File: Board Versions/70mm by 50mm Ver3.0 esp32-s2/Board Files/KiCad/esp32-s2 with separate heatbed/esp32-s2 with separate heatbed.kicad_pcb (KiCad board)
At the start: 2 copper layers, 65.5 x 50 mm, 59 parts, among them IC1 ESP32-S2FN4R2, J1 PJ-037B, J2 USB4520-03-0-A, J3 TB003-500-P02BE, J4 TB003-500-P02BE, J5 Conn_01x03_Male, Q1 PJD25N06A_L2_00001, U1 LD1117S33TR_SOT223, U2 MAX31855KASA, Y1 ECS-400-15-33B-CTN-TR

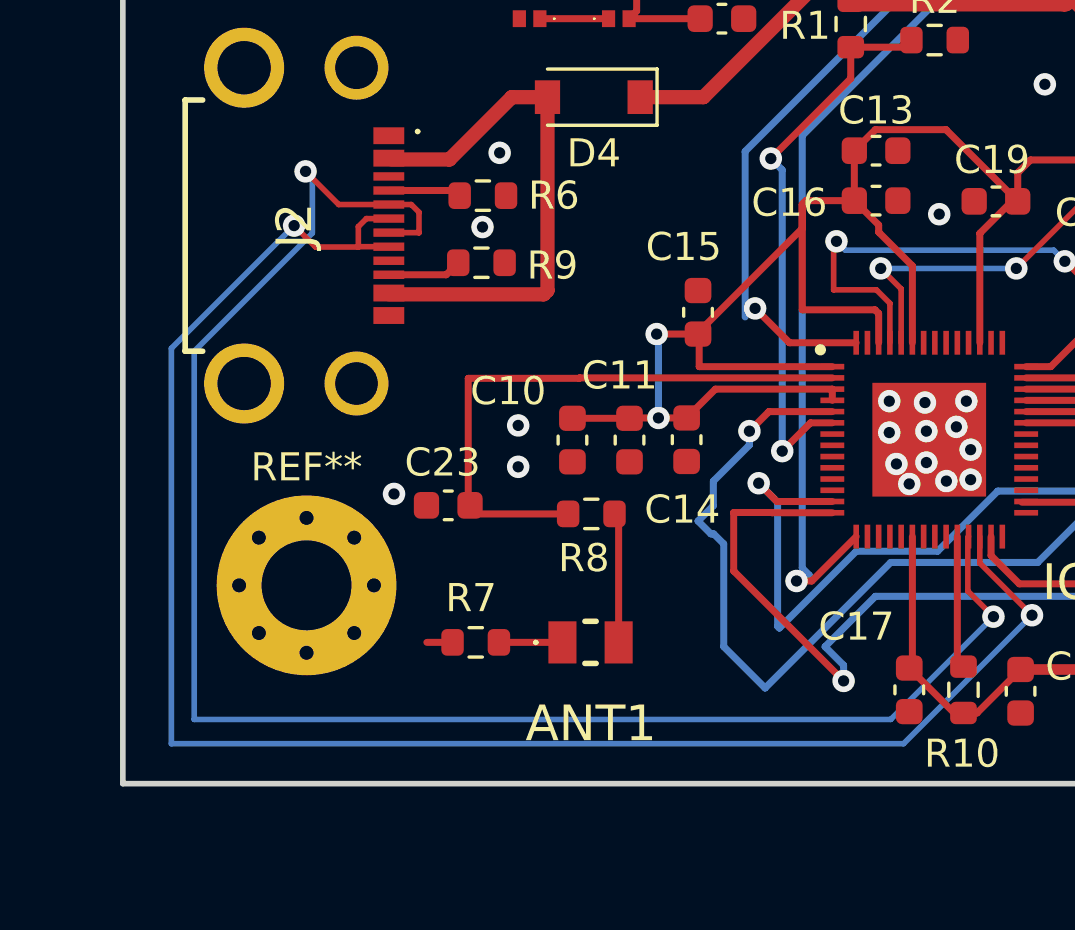
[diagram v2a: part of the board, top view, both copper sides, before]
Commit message: Move antenna to edge
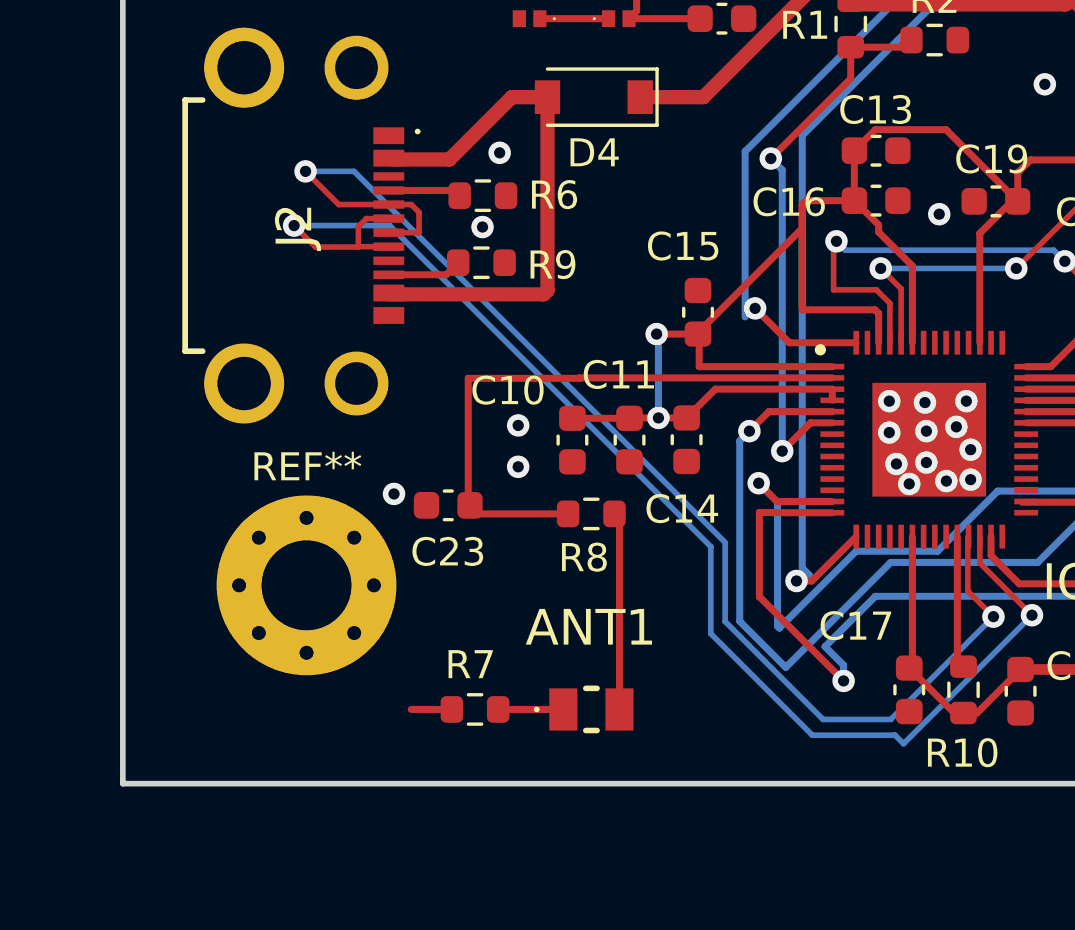
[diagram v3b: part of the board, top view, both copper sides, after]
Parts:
- moved ANT1 2.39 mm to (30.1, 61.4)
- moved R7 2.39 mm to (26.0, 61.4)
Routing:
- net D-: track 61.0 -> 45.4 mm
- net D+: track 62.0 -> 46.8 mm
- net FLASH: track 55.0 -> 52.3 mm
- net Net-(ANT1-Pad2): track 4.63 -> 7.03 mm
- net led2: track 58.2 -> 56.9 mm
- net GND: track 6.17 -> 6.70 mm
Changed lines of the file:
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@@
   )
   (footprint "library_manager:21088321" (layer "F.Cu")
-    (at 30.1084 59.0296)
+    (at 30.1404 61.4172)
     (descr "2108832-1-2")
     (tags "Antenna")
@@
     (property "Sheetname" "")
     (attr smd)
-    (fp_text reference "ANT1" (at 0.016 2.8956) (layer "F.SilkS")
+    (fp_text reference "ANT1" (at -0.016 -2.8956) (layer "F.SilkS")
       (effects (font (size 1.27 1.27) (thickness 0.254)))
     )
@@
       (effects (font (size 1.27 1.27) (thickness 0.254)))
     )
-    (fp_text user "${REFERENCE}" (at 3.7752 -0.0508 90) (layer "F.Fab")
+    (fp_text user "${REFERENCE}" (at 3.6416 -0.4064 90) (layer "F.Fab")
       (effects (font (size 1.27 1.27) (thickness 0.254)))
     )
@@
   )
   (footprint "Resistor_SMD:R_0603_1608Metric" (layer "F.Cu")
-    (at 26.0218 59.0296 180)
+    (at 25.9974 61.4172 180)
     (descr "Resistor SMD 0603 (1608 Metric), square (rectangular) end terminal, IPC_7351 nominal, (Body size source: IPC-SM-782 page 72, https://www.pcb-3d.com/wordpress/wp-content/uploads/ipc-sm-782a_amendment_1_and_2.pdf), generated with kicad-footprint-generator")
     (tags "resistor")
@@
     (property "Sheetname" "")
     (attr smd)
-    (fp_text reference "C23" (at 0.2032 1.524) (layer "F.SilkS")
+    (fp_text reference "C23" (at 0 -1.6764) (layer "F.SilkS")
       (effects (font (size 1 1) (thickness 0.15)))
     )
@@
     (effects (font (size 1.5 1.5) (thickness 0.3)))
   )
-  (segment (start 29.1084 59.0296) (end 26.8468 59.0296) (width 0.25) (layer "F.Cu") (net 1))
-  (segment (start 30.9616 54.4576) (end 31.1084 54.6044) (width 0.25) (layer "F.Cu") (net 2))
-  (segment (start 31.1084 54.6044) (end 31.1084 59.0296) (width 0.25) (layer "F.Cu") (net 2))
+  (segment (start 29.1404 61.4172) (end 26.8224 61.4172) (width 0.25) (layer "F.Cu") (net 1))
+  (segment (start 30.9616 54.4576) (end 31.1404 54.6364) (width 0.25) (layer "F.Cu") (net 2))
+  (segment (start 31.1404 54.6364) (end 31.1404 61.4172) (width 0.25) (layer "F.Cu") (net 2))
   (segment (start 31.75 36.56) (end 31.48 36.83) (width 0.25) (layer "F.Cu") (net 3))
   (segment (start 41.403 28.702) (end 39.37 30.735) (width 1.524) (layer "F.Cu") (net 3))
@@
   (segment (start 32.11 30.86) (end 31.75 30.5) (width 1.27) (layer "F.Cu") (net 3))
   (segment (start 53.608 46.482) (end 53.208 46.482) (width 0.25) (layer "F.Cu") (net 4))
+  (segment (start 25.1724 61.4172) (end 23.7236 61.4172) (width 0.25) (layer "F.Cu") (net 4))
   (segment (start 63.0428 45.9232) (end 62.3824 45.2628) (width 0.25) (layer "F.Cu") (net 4))
-  (segment (start 25.1968 59.0296) (end 24.2824 59.0296) (width 0.25) (layer "F.Cu") (net 4))
   (segment (start 62.3824 44.2468) (end 62.5348 44.0944) (width 0.25) (layer "F.Cu") (net 4))
   (segment (start 53.208 46.482) (end 51.308 44.582) (width 0.25) (layer "F.Cu") (net 4))
@@
   (via (at 35.7632 51.5112) (size 0.8) (drill 0.4) (layers "F.Cu" "B.Cu") (net 17))
   (via (at 63.6016 52.0192) (size 0.8) (drill 0.4) (layers "F.Cu" "B.Cu") (net 17))
-  (segment (start 33.9344 54.7116) (end 34.3916 55.1688) (width 0.25) (layer "B.Cu") (net 17))
+  (segment (start 37.0586 59.9186) (end 40.7924 56.1848) (width 0.25) (layer "B.Cu") (net 17))
+  (segment (start 61.556289 54.064511) (end 63.6016 52.0192) (width 0.25) (layer "B.Cu") (net 17))
+  (segment (start 35.419689 58.279689) (end 37.0586 59.9186) (width 0.25) (layer "B.Cu") (net 17))
+  (segment (start 35.7632 51.5112) (end 35.419689 51.854711) (width 0.25) (layer "B.Cu") (net 17))
+  (segment (start 48.145089 54.064511) (end 61.556289 54.064511) (width 0.25) (layer "B.Cu") (net 17))
+  (segment (start 46.0248 56.1848) (end 48.145089 54.064511) (width 0.25) (layer "B.Cu") (net 17))
+  (segment (start 35.419689 51.854711) (end 35.419689 58.279689) (width 0.25) (layer "B.Cu") (net 17))
   (segment (start 40.7924 56.1848) (end 46.0248 56.1848) (width 0.25) (layer "B.Cu") (net 17))
-  (segment (start 35.7632 51.5112) (end 35.7632 52.006772) (width 0.25) (layer "B.Cu") (net 17))
-  (segment (start 34.3916 55.1688) (end 34.4932 55.1688) (width 0.25) (layer "B.Cu") (net 17))
-  (segment (start 35.7632 52.006772) (end 34.479889 53.290083) (width 0.25) (layer "B.Cu") (net 17))
-  (segment (start 36.322 60.6552) (end 40.7924 56.1848) (width 0.25) (layer "B.Cu") (net 17))
-  (segment (start 48.145089 54.064511) (end 61.556289 54.064511) (width 0.25) (layer "B.Cu") (net 17))
-  (segment (start 34.479889 53.290083) (end 34.479889 54.166111) (width 0.25) (layer "B.Cu") (net 17))
-  (segment (start 34.479889 54.166111) (end 33.9344 54.7116) (width 0.25) (layer "B.Cu") (net 17))
-  (segment (start 61.556289 54.064511) (end 63.6016 52.0192) (width 0.25) (layer "B.Cu") (net 17))
-  (segment (start 34.8488 55.5244) (end 34.8488 59.182) (width 0.25) (layer "B.Cu") (net 17))
-  (segment (start 34.8488 59.182) (end 36.322 60.6552) (width 0.25) (layer "B.Cu") (net 17))
-  (segment (start 46.0248 56.1848) (end 48.145089 54.064511) (width 0.25) (layer "B.Cu") (net 17))
-  (segment (start 34.4932 55.1688) (end 34.8488 55.5244) (width 0.25) (layer "B.Cu") (net 17))
   (segment (start 39.37 38.9636) (end 36.5252 41.8084) (width 0.25) (layer "F.Cu") (net 18))
   (segment (start 39.37 37.845) (end 39.37 38.9636) (width 0.25) (layer "F.Cu") (net 18))
@@
   (segment (start 39.56552 55.78608) (end 36.83 58.5216) (width 0.25) (layer "B.Cu") (net 25))
   (segment (start 68.7324 35.2552) (end 66.7512 35.2552) (width 0.25) (layer "B.Cu") (net 25))
-  (segment (start 35.2044 54.4068) (end 35.2044 56.4896) (width 0.25) (layer "F.Cu") (net 26))
+  (segment (start 36.1188 54.4068) (end 36.1188 57.404) (width 0.25) (layer "F.Cu") (net 26))
+  (segment (start 38.714 54.416) (end 36.5668 54.416) (width 0.25) (layer "F.Cu") (net 26))
   (segment (start 66.6232 39.5224) (end 68.6308 39.5224) (width 0.25) (layer "F.Cu") (net 26))
   (segment (start 68.6308 39.5224) (end 68.7324 39.4208) (width 0.25) (layer "F.Cu") (net 26))
+  (segment (start 36.1188 57.404) (end 39.116 60.4012) (width 0.25) (layer "F.Cu") (net 26))
+  (segment (start 36.5576 54.4068) (end 36.1188 54.4068) (width 0.25) (layer "F.Cu") (net 26))
   (segment (start 36.5668 54.416) (end 36.5576 54.4068) (width 0.25) (layer "F.Cu") (net 26))
-  (segment (start 36.5576 54.4068) (end 35.2044 54.4068) (width 0.25) (layer "F.Cu") (net 26))
-  (segment (start 35.2044 56.4896) (end 39.116 60.4012) (width 0.25) (layer "F.Cu") (net 26))
-  (segment (start 38.714 54.416) (end 36.5668 54.416) (width 0.25) (layer "F.Cu") (net 26))
   (via (at 39.116 60.4012) (size 0.8) (drill 0.4) (layers "F.Cu" "B.Cu") (net 26))
   (via (at 68.7324 39.4208) (size 0.8) (drill 0.4) (layers "F.Cu" "B.Cu") (net 26))
@@
   (via (at 19.9644 42.2656) (size 0.8) (drill 0.4) (layers "F.Cu" "B.Cu") (net 33))
   (segment (start 44.45 58.1152) (end 40.7924 61.7728) (width 0.2) (layer "B.Cu") (net 33))
-  (segment (start 16.002 61.7728) (end 16.002 48.669417) (width 0.2) (layer "B.Cu") (net 33))
-  (segment (start 16.002 48.669417) (end 20.206711 44.464706) (width 0.2) (layer "B.Cu") (net 33))
-  (segment (start 40.7924 61.7728) (end 16.002 61.7728) (width 0.2) (layer "B.Cu") (net 33))
-  (segment (start 20.206711 42.507911) (end 19.9644 42.2656) (width 0.2) (layer "B.Cu") (net 33))
-  (segment (start 20.206711 44.464706) (end 20.206711 42.507911) (width 0.2) (layer "B.Cu") (net 33))
+  (segment (start 34.8996 55.4736) (end 21.6916 42.2656) (width 0.2) (layer "B.Cu") (net 33))
+  (segment (start 21.6916 42.2656) (end 19.9644 42.2656) (width 0.2) (layer "B.Cu") (net 33))
+  (segment (start 40.7924 61.7728) (end 38.38428 61.7728) (width 0.2) (layer "B.Cu") (net 33))
+  (segment (start 34.8996 58.28812) (end 34.8996 55.4736) (width 0.2) (layer "B.Cu") (net 33))
+  (segment (start 38.38428 61.7728) (end 34.8996 58.28812) (width 0.2) (layer "B.Cu") (net 33))
   (segment (start 21.844 44.958) (end 21.856 44.946) (width 0.2) (layer "F.Cu") (net 34))
   (segment (start 22.929 43.946) (end 22.129978 43.946) (width 0.2) (layer "F.Cu") (net 34))
@@
   (via (at 45.8216 58.0644) (size 0.8) (drill 0.4) (layers "F.Cu" "B.Cu") (free) (net 34))
   (via (at 19.558 44.196) (size 0.8) (drill 0.4) (layers "F.Cu" "B.Cu") (net 34))
-  (segment (start 15.1892 62.6364) (end 15.1892 48.5648) (width 0.2) (layer "B.Cu") (net 34))
-  (segment (start 15.1892 48.5648) (end 19.558 44.196) (width 0.2) (layer "B.Cu") (net 34))
-  (segment (start 41.2496 62.6364) (end 15.1892 62.6364) (width 0.2) (layer "B.Cu") (net 34))
+  (segment (start 40.9448 62.3316) (end 37.9984 62.3316) (width 0.2) (layer "B.Cu") (net 34))
+  (segment (start 34.3916 58.7248) (end 34.3916 55.626) (width 0.2) (layer "B.Cu") (net 34))
+  (segment (start 22.9616 44.196) (end 19.558 44.196) (width 0.2) (layer "B.Cu") (net 34))
+  (segment (start 41.2496 62.6364) (end 40.9448 62.3316) (width 0.2) (layer "B.Cu") (net 34))
+  (segment (start 34.3916 55.626) (end 22.9616 44.196) (width 0.2) (layer "B.Cu") (net 34))
+  (segment (start 37.9984 62.3316) (end 34.3916 58.7248) (width 0.2) (layer "B.Cu") (net 34))
   (segment (start 45.8216 58.0644) (end 41.2496 62.6364) (width 0.2) (layer "B.Cu") (net 34))
   (segment (start 54.7212 51.216) (end 45.614 51.216) (width 0.25) (layer "F.Cu") (net 43))
@@
     (polygon
       (pts
-        (xy 24.4348 55.2196)
-        (xy 34.29 55.2196)
-        (xy 34.2392 61.722)
-        (xy 24.4856 61.7728)
+        (xy 24.4348 57.0484)
+        (xy 34.29 57.0484)
+        (xy 34.2392 63.5508)
+        (xy 24.4856 63.6016)
       )
     )

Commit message: Corrections
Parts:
- removed C3: 22uF, Capacitor_SMD:C_0805_2012Metric
- removed C6: 100nF, Capacitor_SMD:C_0603_1608Metric
- added C24: 10nF, Capacitor_SMD:C_0603_1608Metric, F.Cu at (62.8, 23.9)
- C5: value 22uF -> 10uF; footprint Capacitor_SMD:C_0805_2012Metric -> Capacitor_SMD:C_0603_1608Metric
- moved Z1 8.72 mm to (43.1, 25.3)
- moved J3 4.13 mm to (40.3, 18.7)
- moved J4 0.82 mm to (61.0, 18.7)
- moved U2 0.64 mm to (63.8, 27.7)
- moved C8 0.36 mm to (58.6, 28.0)
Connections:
- J4 pad 2: GND -> Net-(J4-Pad2)
- U2 pad 2: GND -> Net-(J4-Pad2)
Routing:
- net Net-(J4-Pad2): track 0.00 -> 13.6 mm
- net VCC: track 49.5 -> 45.1 mm
- net Net-(U2-Pad3): track 10.1 -> 12.9 mm
- net Net-(C7-Pad2): track 21.4 -> 19.0 mm
- net GND: vias 29 -> 30
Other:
- board text added: "39 38 37"
- board text added: "T°C"
